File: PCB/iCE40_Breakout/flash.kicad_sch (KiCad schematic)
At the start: 5 parts, among them J2 prog_hdr, U2 W25Q128JVS

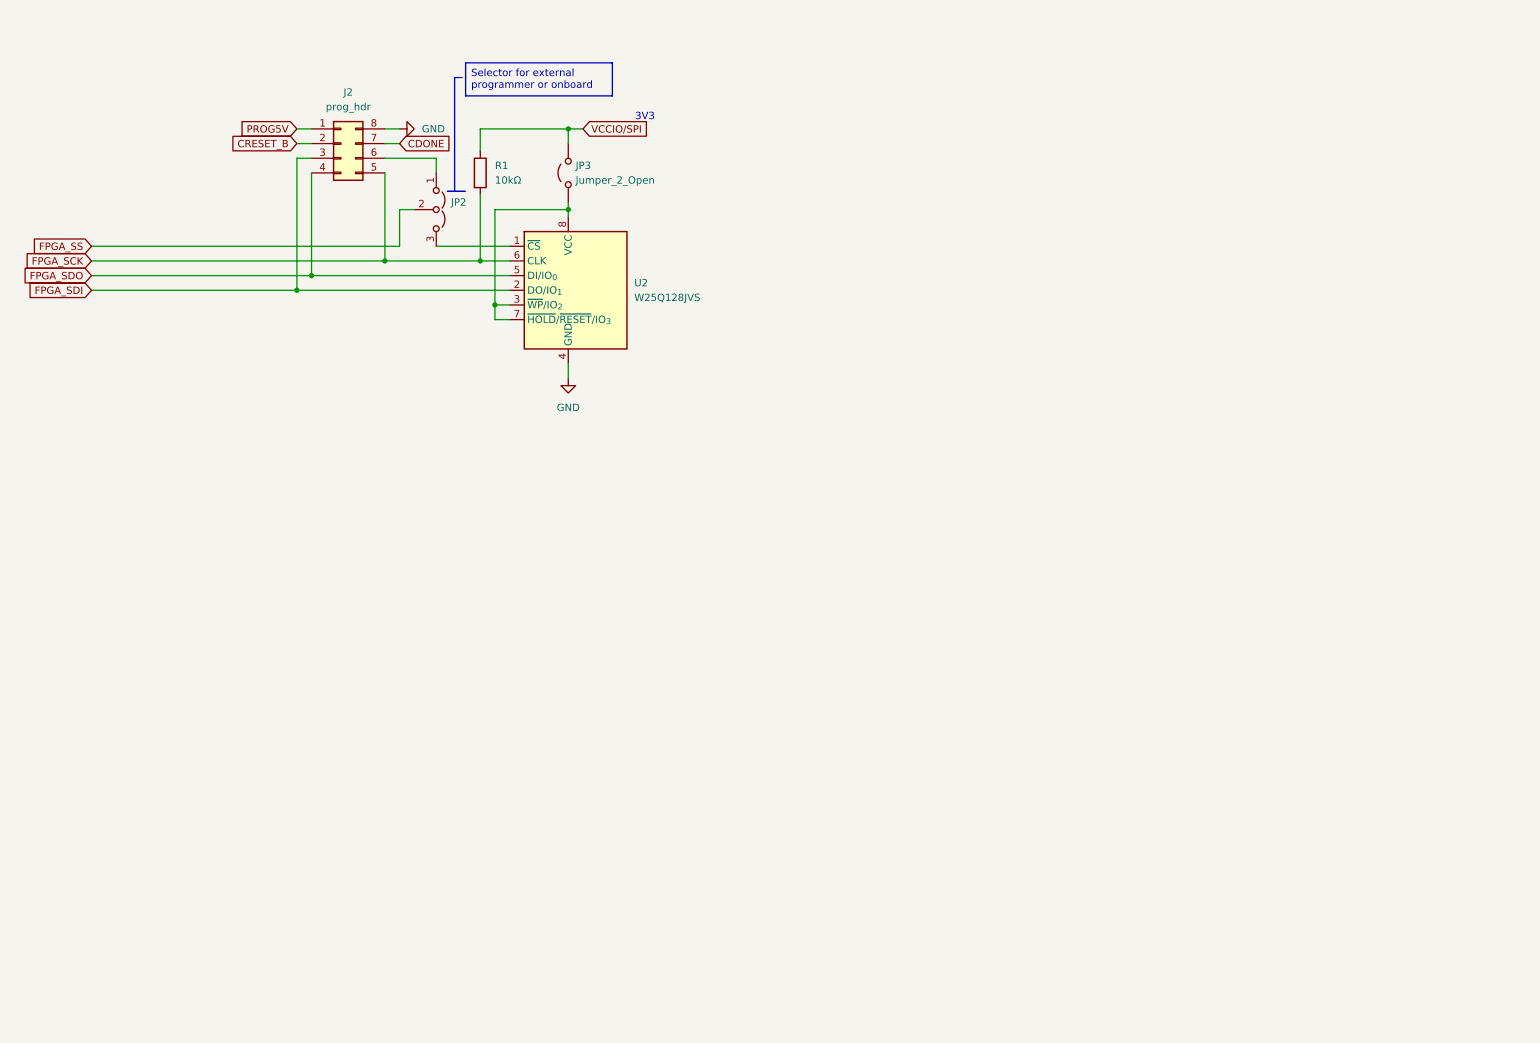
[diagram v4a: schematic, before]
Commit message: Added FT2232HP for USB flash support, and hopefully USB PD
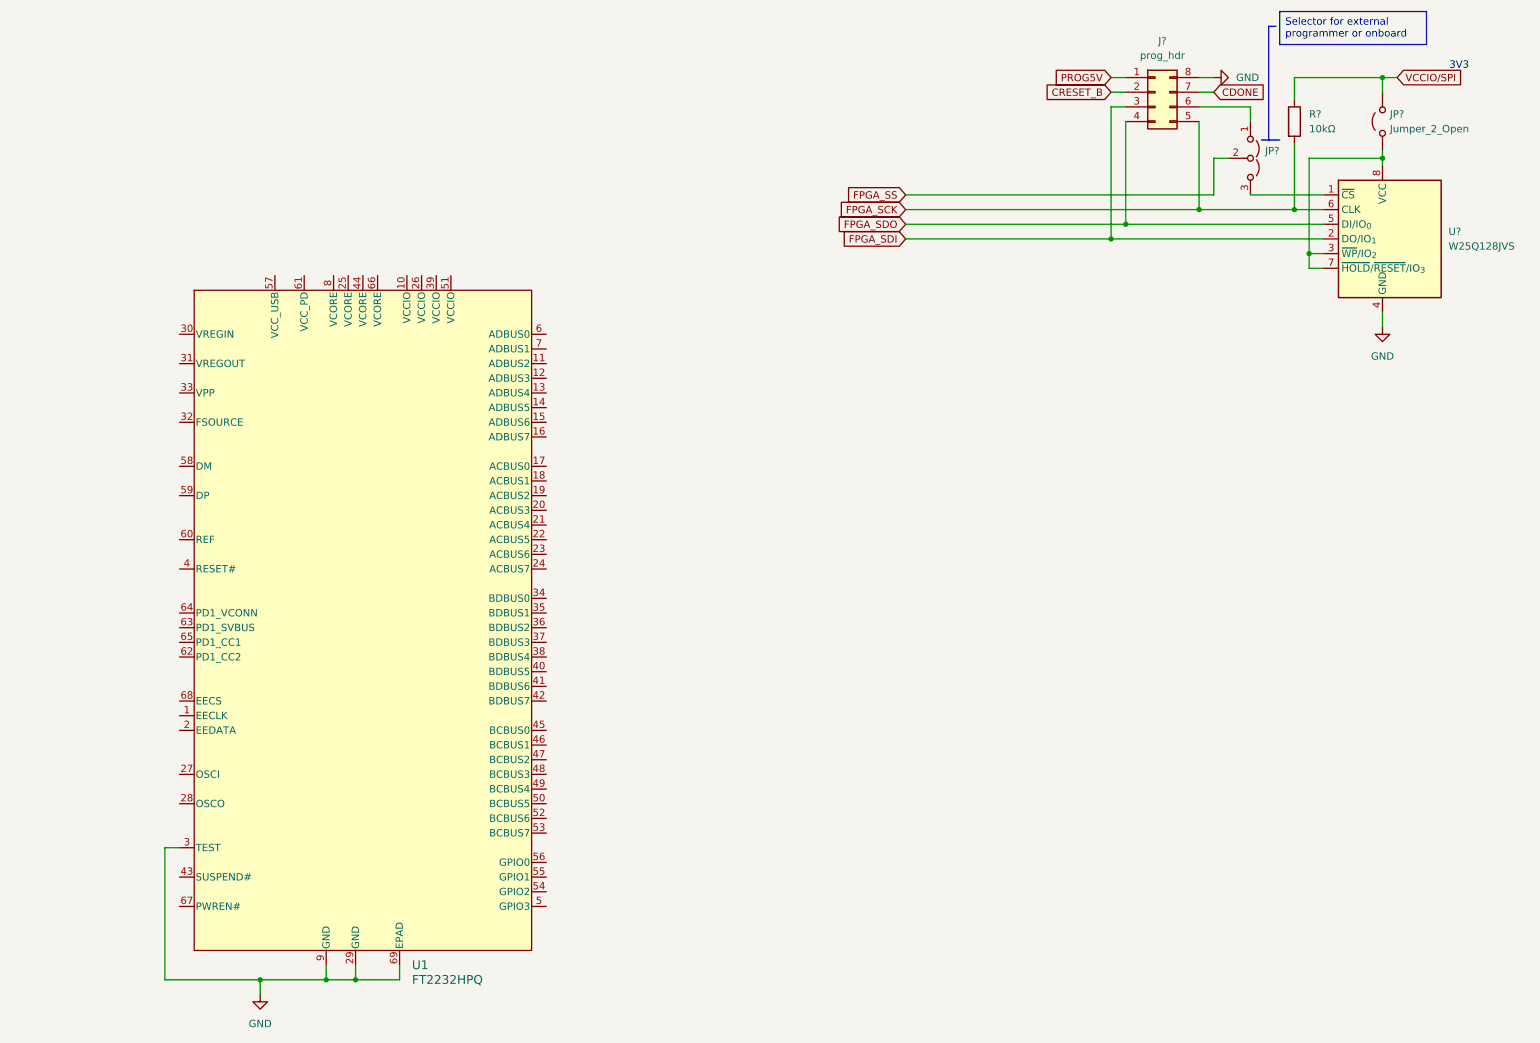
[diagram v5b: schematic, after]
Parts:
- added U1: FT2232HPQ, Interface_FTDI:QFN68_FT2232, symbol Interface_FTDI:FT2232HPQ
- renumbered J2 to J?, JP2 to JP?, JP3 to JP?, R1 to R?, U2 to U?
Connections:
- net GND: now also U1.29 (GND), U1.3 (TEST), U1.69 (EPAD), U1.9 (GND)
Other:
- moved on the sheet: J?, JP?, R?, U?

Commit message: Wired FTDI chip to flash memory, and added power connections
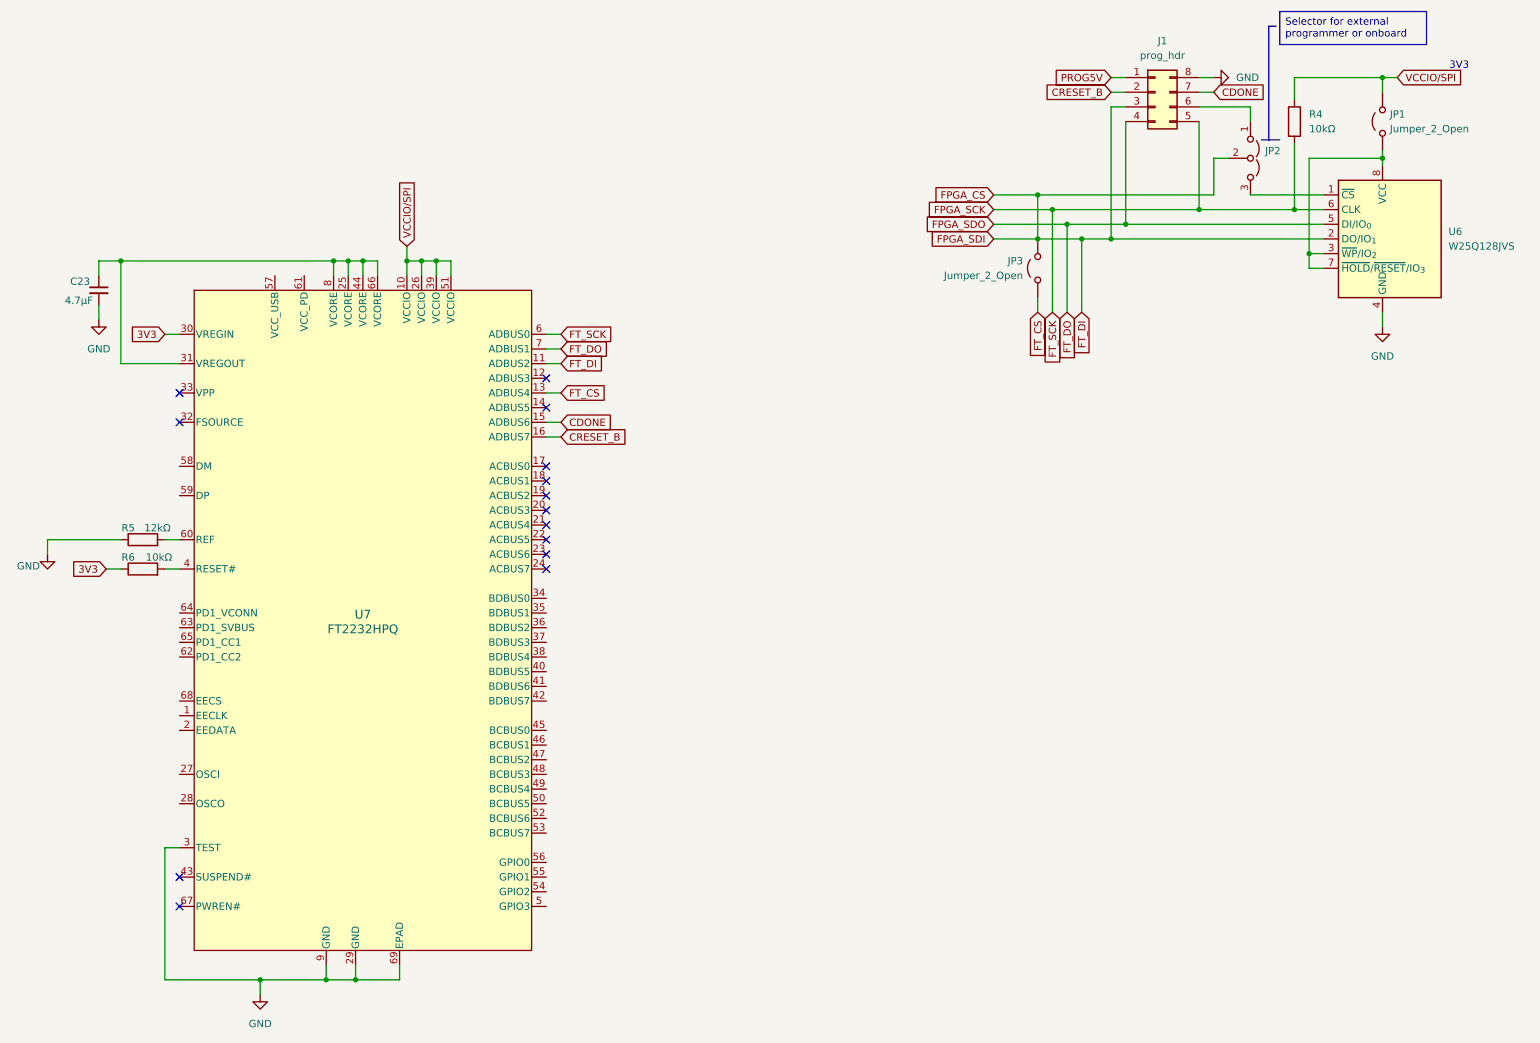
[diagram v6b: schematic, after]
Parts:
- added C23: 4.7μF, Capacitor_SMD:C_0402_1005Metric, symbol Device:C_Small
- added JP3: Jumper_2_Open, Connector_PinSocket_2.54mm:PinSocket_1x02_P2.54mm_Vertical, symbol Jumper:Jumper_2_Open
- added R5: 12kΩ, Resistor_SMD:R_0603_1608Metric, symbol Device:R
- added R6: 10kΩ, Resistor_SMD:R_0603_1608Metric, symbol Device:R
- U7: renamed from U1; LCSC (none) -> C3228146
- gave numbers to parts that had none: 5
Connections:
- net FPGA_SDI is gone; now on net FPGA_CS: J1.3 (Pin_3), U6.2 (DO/IO_{1})
- net FPGA_SS is gone; now on net FPGA_CS: JP2.2 (C)
- net CDONE: now also U7.15 (ADBUS6)
- net CRESET_B: now also U7.16 (ADBUS7)
- net FPGA_SCK: now also U7.6 (ADBUS0)
- net FPGA_SDO: now also U7.7 (ADBUS1)
- net GND: now also C23.2, R5.1
- net VCCIO/SPI: now also U7.10 (VCCIO), U7.26 (VCCIO), U7.39 (VCCIO), U7.51 (VCCIO)
- net FPGA_CS: now reaches U7.11 (ADBUS2)
- net FPGA_CS: now also JP3.1 (A)
- net FT_CS: now reaches U7.13 (ADBUS4)
- net FT_CS: now also JP3.2 (B)
- net at U7.25 (VCORE): now also U7.31 (VREGOUT), U7.44 (VCORE), U7.66 (VCORE), U7.8 (VCORE), C23.1
- net 3V3: now reaches U7.30 (VREGIN)
- net 3V3: now also R6.1
- net at U7.4 (RESET#): now also R6.2
- net at U7.60 (REF): now also R5.2
- no-connect marks 0 -> 14
